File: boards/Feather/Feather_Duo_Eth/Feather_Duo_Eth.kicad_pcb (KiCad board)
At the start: 4 copper layers, 0 parts

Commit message: footprints
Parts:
- added C1: 4.7uF, Capacitor_SMD:C_0603_1608Metric, F.Cu at (237.8, 44.0)
- added C10: 0.1uF, Capacitor_SMD:C_0603_1608Metric, F.Cu at (241.8, 46.5)
- added C101: 22uF, Capacitor_SMD:C_0603_1608Metric, F.Cu at (148.8, 62.0)
- added C102: 0.1uF, Capacitor_SMD:C_0603_1608Metric, F.Cu at (147.2, 62.0)
- added C103: 1uF, Capacitor_SMD:C_0603_1608Metric, F.Cu at (157.2, 81.7)
- added C104: 1uF, Capacitor_SMD:C_0603_1608Metric, F.Cu at (157.2, 83.2)
- added C105: 10uF, Capacitor_SMD:C_0603_1608Metric, F.Cu at (133.2, 73.3)
- added C106: 22uF, Capacitor_SMD:C_0603_1608Metric, F.Cu at (129.9, 62.9)
- added C11: 10uF, Capacitor_SMD:C_0603_1608Metric, F.Cu at (241.8, 49.0)
- added C12: 22nF, Capacitor_SMD:C_0603_1608Metric, F.Cu at (241.8, 51.5)
- added C13: 6.8nF, Capacitor_SMD:C_0603_1608Metric, F.Cu at (241.8, 54.0)
- added C14: 6.8nF, Capacitor_SMD:C_0603_1608Metric, F.Cu at (241.8, 56.5)
- added C15: 10nF, Capacitor_SMD:C_0603_1608Metric, F.Cu at (241.8, 59.0)
- added C16: 1nF, Capacitor_SMD:C_0603_1608Metric, F.Cu at (241.8, 61.6)
- added C17: 0.1uF, Capacitor_SMD:C_0603_1608Metric, F.Cu at (245.8, 44.0)
- added C18: 10uF, Capacitor_SMD:C_0603_1608Metric, F.Cu at (245.8, 46.5)
- added C2: 10nF, Capacitor_SMD:C_0603_1608Metric, F.Cu at (237.8, 46.5)
- added C201: 10uF, Capacitor_SMD:C_0603_1608Metric, B.Cu at (146.8, 66.6)
- added C202: 10nF, Capacitor_SMD:C_0603_1608Metric, B.Cu at (146.8, 69.6)
- added C3: 27pF, Capacitor_SMD:C_0603_1608Metric, F.Cu at (237.8, 49.0)
- added C301: 10uF, Capacitor_SMD:C_0603_1608Metric, B.Cu at (128.8, 67.6)
- added C302: 10nF, Capacitor_SMD:C_0603_1608Metric, B.Cu at (128.8, 70.6)
- added C4: 27pF, Capacitor_SMD:C_0603_1608Metric, F.Cu at (237.8, 51.5)
- added C5: 0.1uF, Capacitor_SMD:C_0603_1608Metric, F.Cu at (237.8, 54.0)
- added C6: 0.1uF, Capacitor_SMD:C_0603_1608Metric, F.Cu at (237.8, 56.5)
- added C7: 0.1uF, Capacitor_SMD:C_0603_1608Metric, F.Cu at (237.8, 59.0)
- added C8: 0.1uF, Capacitor_SMD:C_0603_1608Metric, F.Cu at (237.8, 61.6)
- added C9: 0.1uF, Capacitor_SMD:C_0603_1608Metric, F.Cu at (241.8, 44.0)
- added D101: RED LED, LED_SMD:LED_0603_1608Metric, F.Cu at (136.1, 70.7)
- added D102: ORANGE LED, LED_SMD:LED_0603_1608Metric, F.Cu at (137.7, 70.7)
- added D103: GREEN LED, LED_SMD:LED_0603_1608Metric, F.Cu at (137.7, 61.7)
- added D104: BLUE LED, LED_SMD:LED_0603_1608Metric, F.Cu at (136.1, 61.7)
- added D105: RED LED, LED_SMD:LED_0603_1608Metric, F.Cu at (129.9, 59.9)
- added D106: RED LED, LED_SMD:LED_0603_1608Metric, F.Cu at (184.5, 85.3)
- added D107: ORANGE LED, LED_SMD:LED_0603_1608Metric, F.Cu at (184.5, 87.9)
- added D108: GREEN LED, LED_SMD:LED_0603_1608Metric, F.Cu at (184.5, 90.5)
- added D109: BLUE LED, LED_SMD:LED_0603_1608Metric, F.Cu at (184.5, 93.1)
- added D110: YELLOW LED, LED_SMD:LED_0603_1608Metric, F.Cu at (184.5, 95.7)
- added D111: GREEN LED, LED_SMD:LED_0603_1608Metric, F.Cu at (184.5, 98.2)
- added FB1: FerriteBead_Small, Ferrite_THT:LairdTech_28C0236-0JW-10, F.Cu at (253.7, 47.2)
- added G***: LOGO, memes:doot, F.Cu at (124.0, 66.1)
- added G***: LOGO, memes:doot, B.Cu at (124.0, 66.1)
- added H101: M3, MountingHole:MountingHole_3.2mm_M3_Pad_Via, F.Cu at (156.0, 89.0)
- added H102: M3, MountingHole:MountingHole_3.2mm_M3_Pad_Via, F.Cu at (124.0, 57.1)
- added H103: M3, MountingHole:MountingHole_3.2mm_M3_Pad_Via, F.Cu at (124.2, 88.8)
- added J101: Conn_01x04, Connector_PinHeader_2.54mm:PinHeader_1x04_P2.54mm_Vertical, F.Cu at (133.8, 83.0)
- added J102: Conn_01x04, Connector_PinHeader_2.54mm:PinHeader_1x04_P2.54mm_Vertical, F.Cu at (137.5, 83.0)
- added J103: Conn_01x03, Connector_JST:JST_PH_B3B-PH-K_1x03_P2.00mm_Vertical, F.Cu at (156.7, 77.0)
- added J104: Conn_01x04, Connector_PinHeader_2.54mm:PinHeader_1x04_P2.54mm_Vertical, F.Cu at (141.2, 83.0)
- added J105: Conn_01x04, Connector_PinHeader_2.54mm:PinHeader_1x04_P2.54mm_Vertical, F.Cu at (144.9, 83.0)
- added J106: USB4105-GF-A, Connector_USB:USB_C_Receptacle_GCT_USB4105-xx-A_16P_TopMnt_Horizontal, F.Cu at (123.7, 78.2)
- added J107: Conn_01x04, Connector_PinHeader_2.54mm:PinHeader_1x04_P2.54mm_Vertical, F.Cu at (148.6, 83.0)
- added J107: Conn_01x04, Connector_PinHeader_2.54mm:PinHeader_1x04_P2.54mm_Vertical, F.Cu at (196.0, 82.4)
- added J201: SMA, Connector_Coaxial:SMA_Molex_73251-2120_EdgeMount_Horizontal, B.Cu at (151.0, 55.0)
- added J301: SMA, Connector_Coaxial:SMA_Molex_73251-2120_EdgeMount_Horizontal, B.Cu at (133.0, 55.0)
- added L201: 330nH, Inductor_SMD:L_0603_1608Metric, B.Cu at (151.8, 59.8)
- added L301: 330nH, Inductor_SMD:L_0603_1608Metric, B.Cu at (133.8, 59.8)
- added R1: 12.4k, Resistor_SMD:R_0603_1608Metric, F.Cu at (245.8, 49.0)
- added R10: 49.9, Resistor_SMD:R_0603_1608Metric, F.Cu at (249.8, 51.5)
- added R101: 20k, Resistor_SMD:R_0603_1608Metric, F.Cu at (157.2, 80.2)
- added R102: 1k, Resistor_SMD:R_0603_1608Metric, F.Cu at (136.1, 67.7)
- added R103: 1k, Resistor_SMD:R_0603_1608Metric, F.Cu at (137.7, 67.7)
- added R104: 1k, Resistor_SMD:R_0603_1608Metric, F.Cu at (137.7, 64.7)
- added R105: 1k, Resistor_SMD:R_0603_1608Metric, F.Cu at (136.1, 64.7)
- added R106: 5.1k, Resistor_SMD:R_0603_1608Metric, F.Cu at (131.9, 76.3)
- added R107: 5.1k, Resistor_SMD:R_0603_1608Metric, F.Cu at (130.0, 81.3)
- added R108: 1k, Resistor_SMD:R_0603_1608Metric, F.Cu at (129.9, 61.4)
- added R109: 1k, Resistor_SMD:R_0603_1608Metric, F.Cu at (188.6, 85.3)
- added R110: 1k, Resistor_SMD:R_0603_1608Metric, F.Cu at (188.6, 87.8)
- added R111: 1k, Resistor_SMD:R_0603_1608Metric, F.Cu at (188.6, 90.3)
- added R112: 1k, Resistor_SMD:R_0603_1608Metric, F.Cu at (188.6, 92.8)
- added R113: 1k, Resistor_SMD:R_0603_1608Metric, F.Cu at (188.6, 95.3)
- added R114: 1k, Resistor_SMD:R_0603_1608Metric, F.Cu at (188.6, 97.8)
- added R2: 33, Resistor_SMD:R_0603_1608Metric, F.Cu at (245.8, 51.5)
- added R3: 33, Resistor_SMD:R_0603_1608Metric, F.Cu at (245.8, 54.0)
- added R4: 33, Resistor_SMD:R_0603_1608Metric, F.Cu at (245.8, 56.5)
- added R5: 33, Resistor_SMD:R_0603_1608Metric, F.Cu at (245.8, 59.0)
- added R6: 49.9, Resistor_SMD:R_0603_1608Metric, F.Cu at (245.8, 61.6)
- added R7: 49.9, Resistor_SMD:R_0603_1608Metric, F.Cu at (249.8, 44.0)
- added R8: 10, Resistor_SMD:R_0603_1608Metric, F.Cu at (249.8, 46.5)
- added R9: 49.9, Resistor_SMD:R_0603_1608Metric, F.Cu at (249.8, 49.0)
- added U1: W5500, Package_QFP:LQFP-48_7x7mm_P0.5mm, F.Cu at (196.2, 101.9)
- added U101: ESP32-S3-MINI-1U, RF_Module:ESP32-S2-MINI-1U, F.Cu at (146.6, 71.5)
- added U102: ECMF02-2AMX6, Package_DFN_QFN:ST_UQFN-6L_1.5x1.7mm_P0.5mm, F.Cu at (129.7, 78.4)
- added U103: AMS1117-3.3, Package_TO_SOT_SMD:SOT-223-3_TabPin2, F.Cu at (131.6, 68.1)
- added U201: E22-400MM22S, RF_Module_Ebyte:E22-400MM22S, B.Cu at (153.5, 66.1)
- added U301: E22-400MM22S, RF_Module_Ebyte:E22-400MM22S, B.Cu at (135.5, 66.1)
- added Y2: Crystal_GND24, Crystal:Crystal_SMD_3225-4Pin_3.2x2.5mm, F.Cu at (254.4, 53.9)
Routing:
- net /BOOT: track 0.00 -> 22.1 mm, vias 0 -> 1
- net +3V3: track 0.00 -> 20.1 mm, vias 0 -> 10
- net /E22_CS_0: track 0.00 -> 17.3 mm, vias 0 -> 2
- net +5V: track 0.00 -> 15.4 mm, vias 0 -> 2
- net /SPI_SCK_0: track 0.00 -> 14.8 mm, vias 0 -> 1
- net /E22_TXEN_1: track 0.00 -> 14.3 mm, vias 0 -> 1
- net /E22_RESET_1: track 0.00 -> 14.2 mm, vias 0 -> 1
- net /E22_RXEN_0: track 0.00 -> 14.0 mm, vias 0 -> 1
- net /IO46: track 0.00 -> 13.7 mm
- net /E22_TXEN_0: track 0.00 -> 13.6 mm, vias 0 -> 1
- net /E22_RXEN_1: track 0.00 -> 13.4 mm, vias 0 -> 1
- net /E22_DI02_0: track 0.00 -> 12.2 mm, vias 0 -> 1
- net /USB_D-: track 0.00 -> 12.2 mm
- net /USB_D+: track 0.00 -> 12.2 mm
- net /RESET: track 0.00 -> 12.1 mm
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- added copper zone on F.Cu, net +3V3
- added copper zone on In1.Cu, net +3V3
- added copper zone on B.Cu, net GND
- added copper zone on F.Cu, net GND
- added copper zone on In2.Cu, net GND
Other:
- board outline added: 40 x 40 mm
- board text added: "3V3"
- board text added: "Duo"
- board text added: "Feather"
- board text added: "GND"
- board text added: "JLCJLCJLCJLC"
- board text added: "Nicholas Phillips Thomas McManamen"
- board text added: "TX RX"

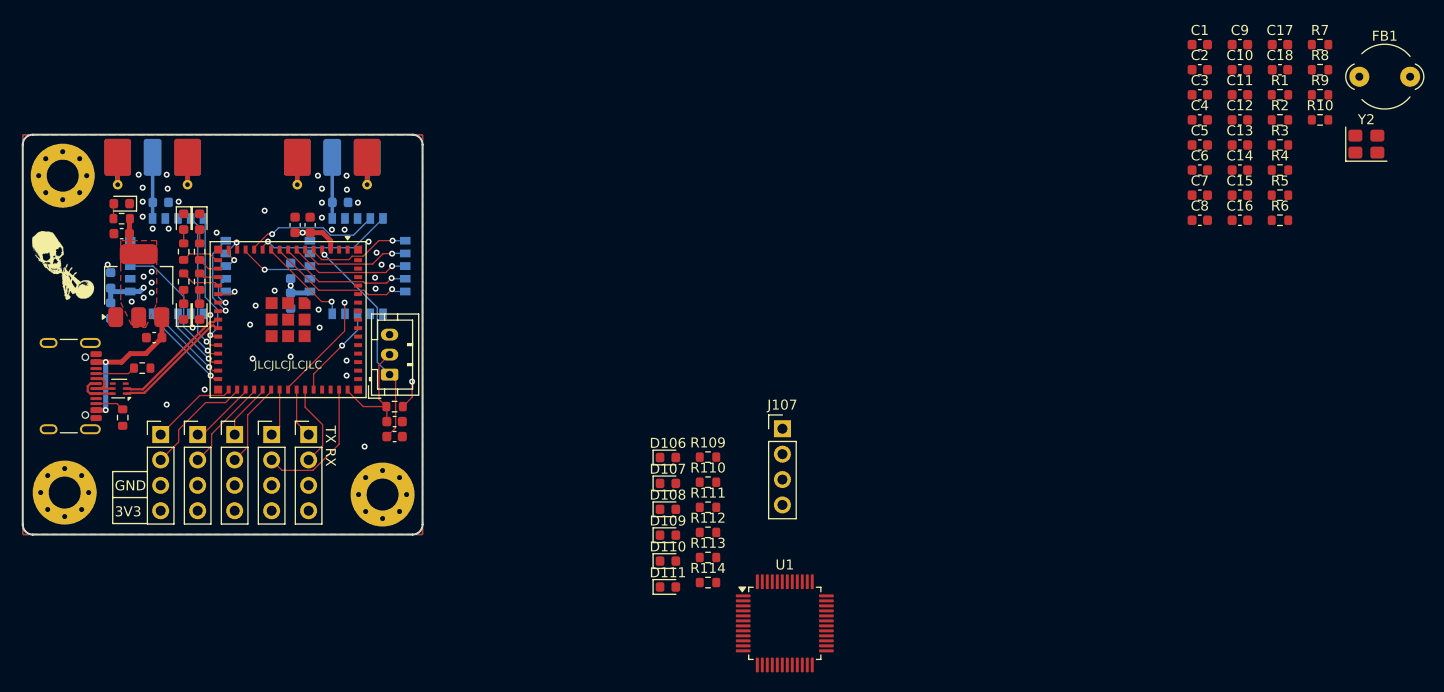
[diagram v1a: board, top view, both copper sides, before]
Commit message: Connector layout changes
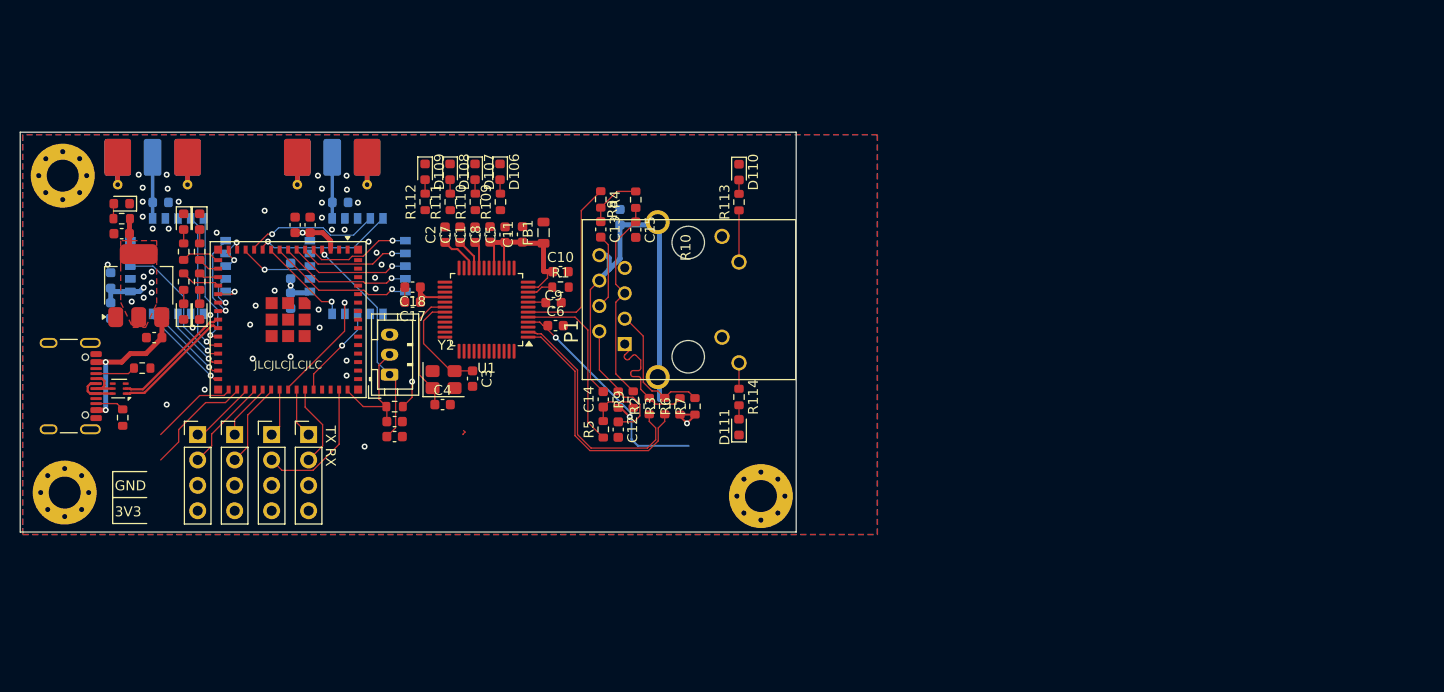
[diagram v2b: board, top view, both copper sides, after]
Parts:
- removed G*** (x2): LOGO, memes:doot
- removed J101: Conn_01x04, Connector_PinHeader_2.54mm:PinHeader_1x04_P2.54mm_Vertical
- removed the J107 at (196.0, 82.4)
- added P1: J1B1211CCD, FerriteBead:J1B1211CCD, F.Cu at (186.6, 69.5)
- C16: moved to B.Cu
- FB1: footprint Ferrite_THT:LairdTech_28C0236-0JW-10 -> Inductor_SMD:L_0805_2012Metric
- moved Y2 95.3 mm to (162.1, 77.5)
- moved C17 90.5 mm to (159.0, 69.8), turned to 180 degrees
- moved C18 89.5 mm to (159.0, 68.2), turned to 180 degrees
- moved FB1 83.1 mm to (172.1, 62.8), turned to 90 degrees
- moved C4 80.9 mm to (162.0, 80.0)
- moved C3 78.1 mm to (165.0, 77.4), turned to -90 degrees
- moved R8 77.6 mm to (179.6, 79.5), turned to 90 degrees
- moved C2 77.3 mm to (162.2, 63.0), turned to 90 degrees
- moved R9 75.2 mm to (181.1, 79.5), turned to 90 degrees
- moved C1 75.0 mm to (165.2, 63.0), turned to 90 degrees
- moved R1 74.5 mm to (173.8, 68.2)
- moved C7 74.1 mm to (163.8, 63.0), turned to 90 degrees
- moved C9 73.4 mm to (173.1, 69.8)
- moved C11 73.1 mm to (170.0, 63.0), turned to 90 degrees
- moved R7 72.2 mm to (187.2, 80.2), turned to 90 degrees
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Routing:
- net +3V3A: track 0.00 -> 52.2 mm, vias 0 -> 3
- net CHASSIS_GND: track 0.00 -> 30.9 mm
- net /TXN: track 0.00 -> 24.8 mm
- net /TXP: track 0.00 -> 24.5 mm
- net Net-(P1-RCT): track 0.00 -> 20.6 mm
- net /RXP: track 0.00 -> 17.9 mm
- net /RXN: track 0.00 -> 17.9 mm
- net Net-(P1-TD-): track 0.00 -> 13.5 mm
- net Net-(P1-TCT): track 0.00 -> 13.2 mm
- net Net-(P1-TD+): track 0.00 -> 13.1 mm
- net Net-(U1-XI/CLKIN): track 0.00 -> 12.2 mm
- net Net-(P1-RD-): track 0.00 -> 12.0 mm
- net /W5500_INT: track 0.00 -> 11.4 mm
- net /IO36: track 11.4 -> 0.00 mm
- net Net-(U1-XO): track 0.00 -> 10.8 mm
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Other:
- board size 40 x 40 mm -> 77.6 x 40 mm
